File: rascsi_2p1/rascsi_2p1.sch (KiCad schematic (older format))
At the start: 92 parts, among them IC1 SN74LS245DW, IC2 SN74LS245DW, IC3 SN74LS245DW, IC4 SN74LS245DW, J1 Raspberry_Pi_2_3, J2 Conn_01x02_Male, J3 Conn_02x25_Odd_Even, J4 I2C Pinout, J5 L717SDB25PA4CH4F, X1 Mac, X2 Dogcow, X3 Mac2, X4 Raspberry Pi, X5 Dogcow2, X6 Mac Trashcan, X7 Pi, X8 Pi

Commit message: Generated gerber files, part lists and re-generated schematic
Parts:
- D1, D2, D3, D4, D6: value LED_Small -> Green; LCSC (none) -> C2297
- D5: LCSC (none) -> C2297
- D7: LCSC (none) -> C162734; LSCS C162734 -> (none)
- FUSE1: LCSC (none) -> C182974; LSCS C182974 -> (none)
- R3, R5, R6: value 147 -> 120; LCSC C64531 -> C25079
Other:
- note added: "01-Aug-2020"
- note added: "2.1"
- note added: "Change direction based \nupon the IND signal"
- note added: "Change direction based \nupon the TAD signal"
- note added: "RaSCSI - 68kmla Edition"
- note removed: "DIR = +5v\nA is input, B is output"
- note removed: "DIR = GND\nB is input, A is output"
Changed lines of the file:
@@
 EESchema Schematic File Version 4
+LIBS:rascsi_2p1-cache
 EELAYER 30 0
 EELAYER END
@@
 F 2 "Diode_SMD:D_SOD-123" H 4300 1950 50  0001 C CNN
 F 3 "" H 4300 1950 50  0001 C CNN
-F 4 "C162734" H 4300 1950 50  0001 C CNN "LSCS"
+F 4 "C162734" H 4300 1950 50  0001 C CNN "LCSC"
 	1    4300 1950
 	-1   0    0    1
@@
 F 2 "Fuse:Fuse_1206_3216Metric" H 4000 1950 50  0001 C CNN
 F 3 "" H 4000 1950 50  0001 C CNN
-F 4 "C182974" H 4000 1950 50  0001 C CNN "LSCS"
+F 4 "C182974" H 4000 1950 50  0001 C CNN "LCSC"
 	1    4000 1950
 	-1   0    0    1
@@
 P 750 1400
 F 0 "D1" V 796 1330 50  0000 R CNN
-F 1 "LED_Small" V 705 1330 50  0000 R CNN
+F 1 "Green" V 705 1330 50  0000 R CNN
 F 2 "LED_SMD:LED_0805_2012Metric" V 750 1400 50  0001 C CNN
 F 3 "~" V 750 1400 50  0001 C CNN
+F 4 "C2297" V 750 1400 50  0001 C CNN "LCSC"
 	1    750  1400
 	0    -1   -1   0
@@
 P 1200 1400
 F 0 "D2" V 1246 1330 50  0000 R CNN
-F 1 "LED_Small" V 1155 1330 50  0000 R CNN
+F 1 "Green" V 1155 1330 50  0000 R CNN
 F 2 "LED_SMD:LED_0805_2012Metric" V 1200 1400 50  0001 C CNN
 F 3 "~" V 1200 1400 50  0001 C CNN
+F 4 "C2297" V 1200 1400 50  0001 C CNN "LCSC"
 	1    1200 1400
 	0    -1   -1   0
@@
 P 1700 1400
 F 0 "D3" V 1746 1330 50  0000 R CNN
-F 1 "LED_Small" V 1655 1330 50  0000 R CNN
+F 1 "Green" V 1655 1330 50  0000 R CNN
 F 2 "LED_SMD:LED_0805_2012Metric" V 1700 1400 50  0001 C CNN
 F 3 "~" V 1700 1400 50  0001 C CNN
+F 4 "C2297" V 1700 1400 50  0001 C CNN "LCSC"
 	1    1700 1400
 	0    -1   -1   0
@@
 P 2150 1400
 F 0 "D4" V 2196 1330 50  0000 R CNN
-F 1 "LED_Small" V 2105 1330 50  0000 R CNN
+F 1 "Green" V 2105 1330 50  0000 R CNN
 F 2 "LED_SMD:LED_0805_2012Metric" V 2150 1400 50  0001 C CNN
 F 3 "~" V 2150 1400 50  0001 C CNN
+F 4 "C2297" V 2150 1400 50  0001 C CNN "LCSC"
 	1    2150 1400
 	0    -1   -1   0
@@
 Change direction based upon PI-DTD
 Text Notes 7900 5600 1    50   ~ 0
-DIR = GND\nB is input, A is output
+Change direction based \nupon the IND signal
 Text Notes 7950 4200 1    50   ~ 0
-DIR = +5v\nA is input, B is output
+Change direction based \nupon the TAD signal
 Wire Notes Line
 	8300 4850 10200 4850
@@
 P 4100 1600
 F 0 "D6" V 4146 1530 50  0000 R CNN
-F 1 "LED_Small" V 4055 1530 50  0001 R CNN
+F 1 "Green" V 4055 1530 50  0001 R CNN
 F 2 "LED_SMD:LED_0805_2012Metric" V 4100 1600 50  0001 C CNN
 F 3 "~" V 4100 1600 50  0001 C CNN
+F 4 "C2297" V 4100 1600 50  0001 C CNN "LCSC"
 	1    4100 1600
 	-1   0    0    1
@@
 P 3900 1350
 F 0 "R5" H 3959 1396 50  0000 L CNN
-F 1 "147" H 3959 1305 50  0000 L CNN
+F 1 "120" H 3959 1305 50  0000 L CNN
 F 2 "Resistor_SMD:R_0402_1005Metric" H 3900 1350 50  0001 C CNN
 F 3 "https://datasheet.lcsc.com/szlcsc/Uniroyal-Elec-0402WGF1470TCE_C64531.pdf" H 3900 1350 50  0001 C CNN
-F 4 "C64531" H 3900 1350 50  0001 C CNN "LCSC"
+F 4 "C25079" H 3900 1350 50  0001 C CNN "LCSC"
 	1    3900 1350
 	0    -1   -1   0
@@
 F 2 "LED_SMD:LED_0805_2012Metric" V 4100 1350 50  0001 C CNN
 F 3 "~" V 4100 1350 50  0001 C CNN
+F 4 "C2297" V 4100 1350 50  0001 C CNN "LCSC"
 	1    4100 1350
 	-1   0    0    1
@@
 P 3900 1600
 F 0 "R6" H 3959 1646 50  0000 L CNN
-F 1 "147" H 3959 1555 50  0000 L CNN
+F 1 "120" H 3959 1555 50  0000 L CNN
 F 2 "Resistor_SMD:R_0402_1005Metric" H 3900 1600 50  0001 C CNN
 F 3 "https://datasheet.lcsc.com/szlcsc/Uniroyal-Elec-0402WGF1470TCE_C64531.pdf" H 3900 1600 50  0001 C CNN
-F 4 "C64531" H 3900 1600 50  0001 C CNN "LCSC"
+F 4 "C25079" H 3900 1600 50  0001 C CNN "LCSC"
 	1    3900 1600
 	0    -1   -1   0
@@
 P 1700 1200
 F 0 "R3" H 1759 1246 50  0000 L CNN
-F 1 "147" H 1759 1155 50  0000 L CNN
+F 1 "120" H 1759 1155 50  0000 L CNN
 F 2 "Resistor_SMD:R_0402_1005Metric" H 1700 1200 50  0001 C CNN
 F 3 "https://datasheet.lcsc.com/szlcsc/Uniroyal-Elec-0402WGF1470TCE_C64531.pdf" H 1700 1200 50  0001 C CNN
-F 4 "C64531" H 1700 1200 50  0001 C CNN "LCSC"
+F 4 "C25079" H 1700 1200 50  0001 C CNN "LCSC"
 	1    1700 1200
 	1    0    0    -1
@@
 Wire Notes Line
 	2700 550  2700 2450
+Text Notes 6750 7760 0    87   ~ 17
+RaSCSI - 68kmla Edition
+Text Notes 9900 7890 0    79   ~ 16
+2.1
+Text Notes 7450 7870 0    59   ~ 12
+01-Aug-2020
 $EndSCHEMATC

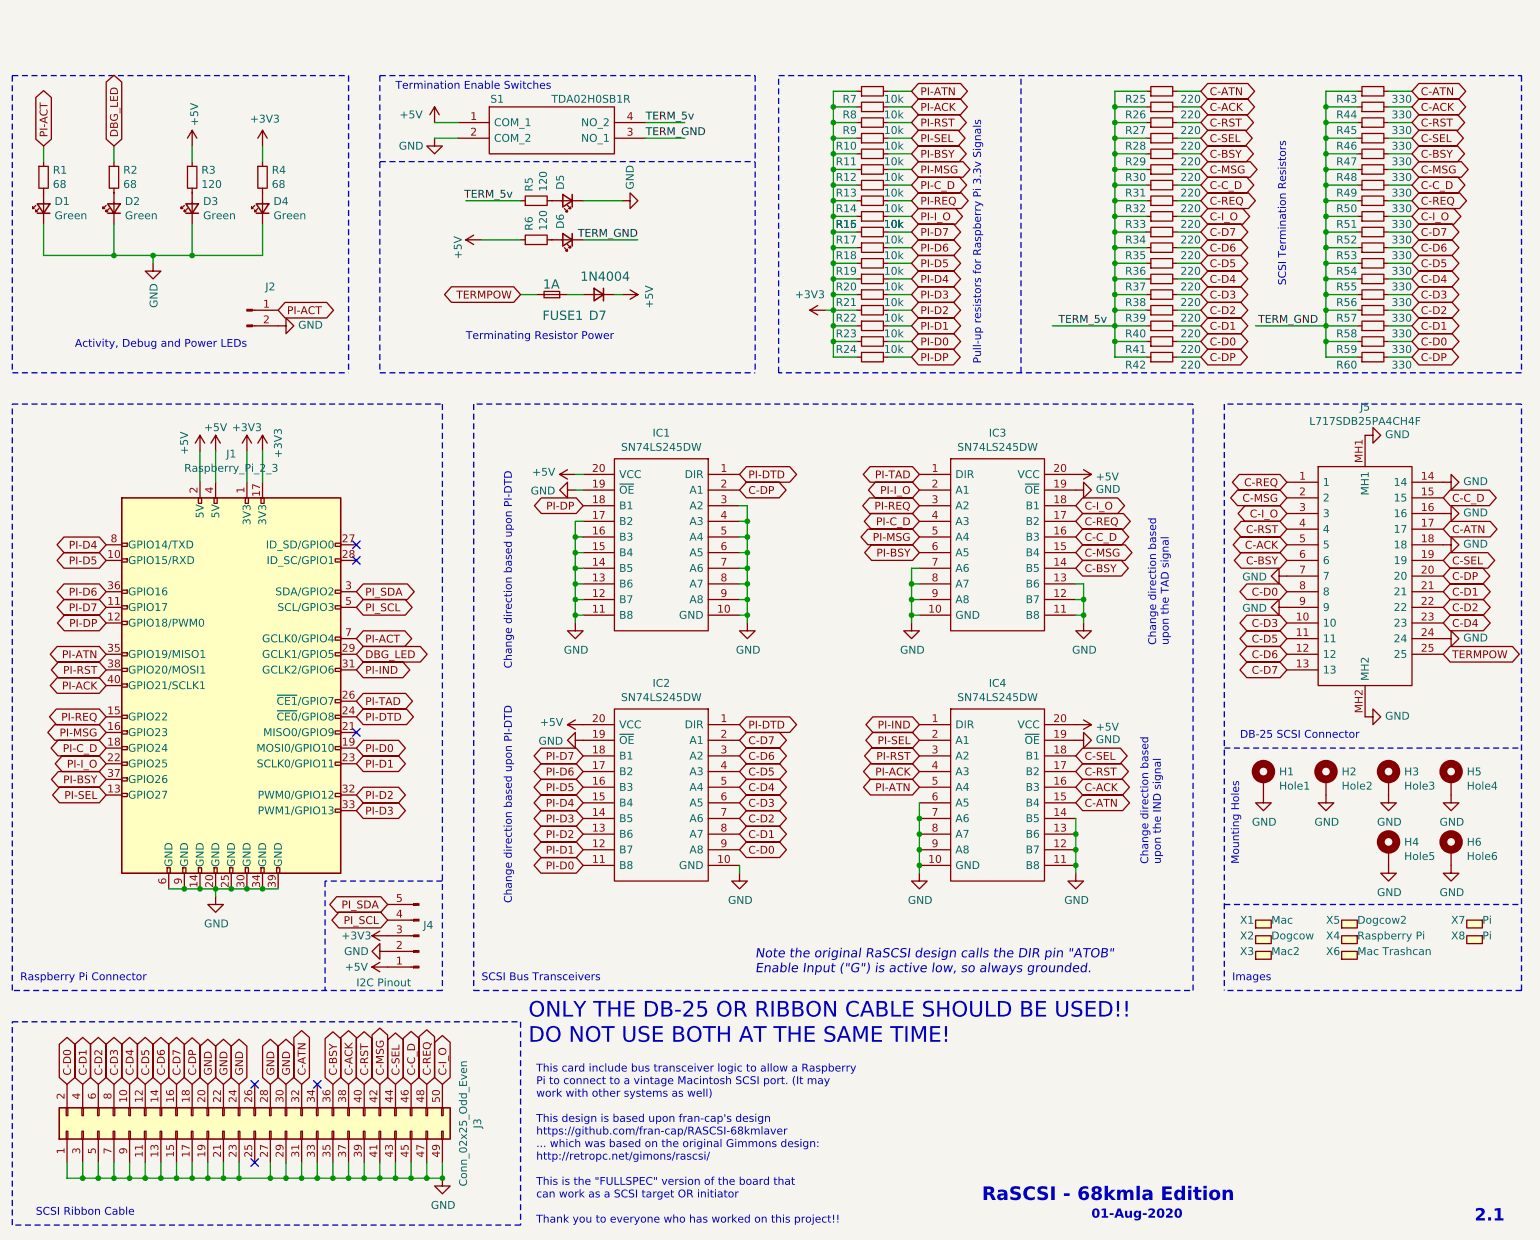
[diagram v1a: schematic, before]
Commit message: Fixed orientation of termpwr diode. Updated to version "2.1a"
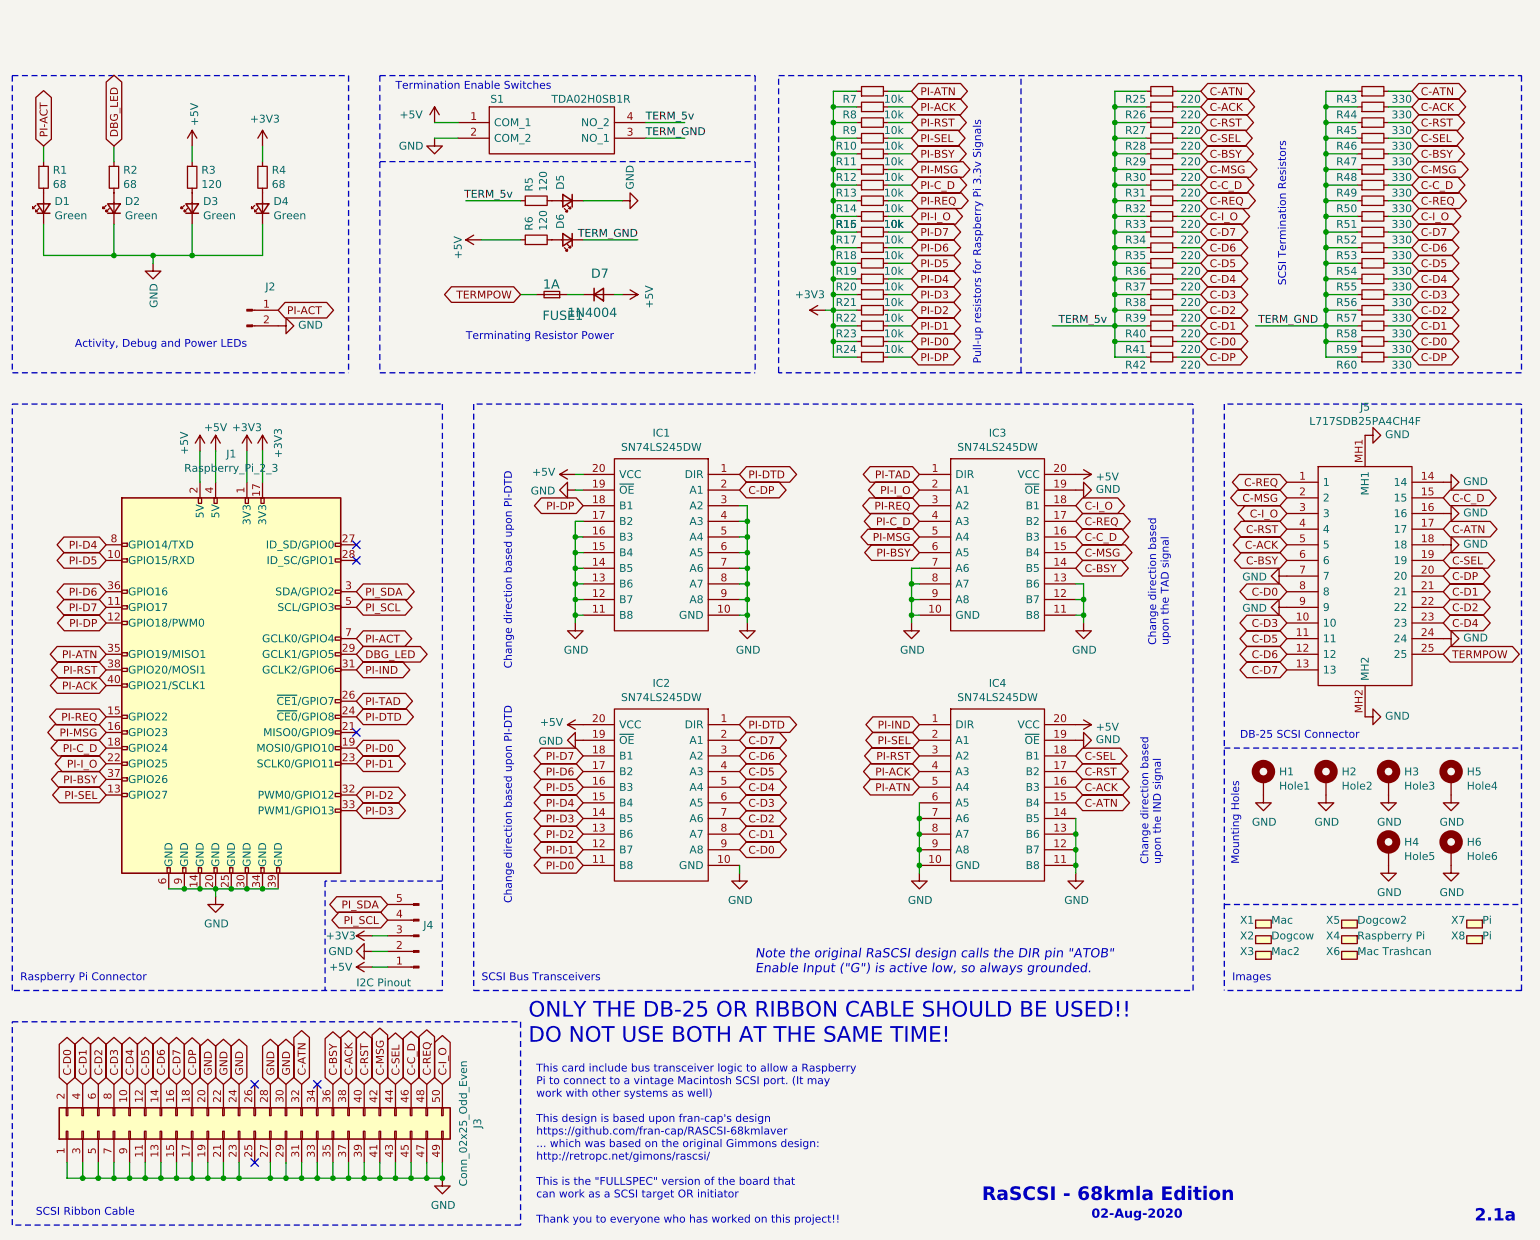
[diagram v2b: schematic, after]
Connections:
- net +5V: now also D7.2 (A); no longer D7.1 (K)
- net at FUSE1.1: now also D7.1 (K); no longer D7.2 (A)
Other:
- note added: "02-Aug-2020"
- note added: "2.1a"
- note removed: "01-Aug-2020"
- note removed: "2.1"
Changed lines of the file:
@@
 EESchema Schematic File Version 4
-LIBS:rascsi_2p1-cache
 EELAYER 30 0
 EELAYER END
@@
 F 4 "C162734" H 4300 1950 50  0001 C CNN "LCSC"
 	1    4300 1950
-	-1   0    0    1
+	1    0    0    -1
 $EndComp
 $Comp
@@
 L power:+5V #PWR012
 U 1 1 5F0B94FB
-P 2950 6250
-F 0 "#PWR012" H 2950 6100 50  0001 C CNN
-F 1 "+5V" V 2950 6450 50  0000 C CNN
-F 2 "" H 2950 6250 50  0001 C CNN
-F 3 "" H 2950 6250 50  0001 C CNN
-	1    2950 6250
+P 2850 6250
+F 0 "#PWR012" H 2850 6100 50  0001 C CNN
+F 1 "+5V" V 2850 6450 50  0000 C CNN
+F 2 "" H 2850 6250 50  0001 C CNN
+F 3 "" H 2850 6250 50  0001 C CNN
+	1    2850 6250
 	0    -1   -1   0
 $EndComp
@@
 L power:GND #PWR011
 U 1 1 5F0B9E0E
-P 2950 6150
-F 0 "#PWR011" H 2950 5900 50  0001 C CNN
-F 1 "GND" V 2950 5950 50  0000 C CNN
-F 2 "" H 2950 6150 50  0001 C CNN
-F 3 "" H 2950 6150 50  0001 C CNN
-	1    2950 6150
+P 2850 6150
+F 0 "#PWR011" H 2850 5900 50  0001 C CNN
+F 1 "GND" V 2850 5950 50  0000 C CNN
+F 2 "" H 2850 6150 50  0001 C CNN
+F 3 "" H 2850 6150 50  0001 C CNN
+	1    2850 6150
 	0    1    1    0
 $EndComp
@@
 L power:+3V3 #PWR010
 U 1 1 5F0BA39A
-P 2950 6050
-F 0 "#PWR010" H 2950 5900 50  0001 C CNN
-F 1 "+3V3" V 2950 6250 50  0000 C CNN
-F 2 "" H 2950 6050 50  0001 C CNN
-F 3 "" H 2950 6050 50  0001 C CNN
-	1    2950 6050
+P 2850 6050
+F 0 "#PWR010" H 2850 5900 50  0001 C CNN
+F 1 "+3V3" V 2850 6250 50  0000 C CNN
+F 2 "" H 2850 6050 50  0001 C CNN
+F 3 "" H 2850 6050 50  0001 C CNN
+	1    2850 6050
 	0    -1   -1   0
 $EndComp
@@
 RaSCSI - 68kmla Edition
 Text Notes 9900 7890 0    79   ~ 16
-2.1
+2.1a
 Text Notes 7450 7870 0    59   ~ 12
-01-Aug-2020
+02-Aug-2020
+Wire Wire Line
+	2850 6050 2950 6050
+Wire Wire Line
+	2950 6150 2850 6150
+Wire Wire Line
+	2850 6250 2950 6250
 $EndSCHEMATC
